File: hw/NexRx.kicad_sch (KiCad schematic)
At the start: 14 parts, among them J101 SMA, T101 INPUT

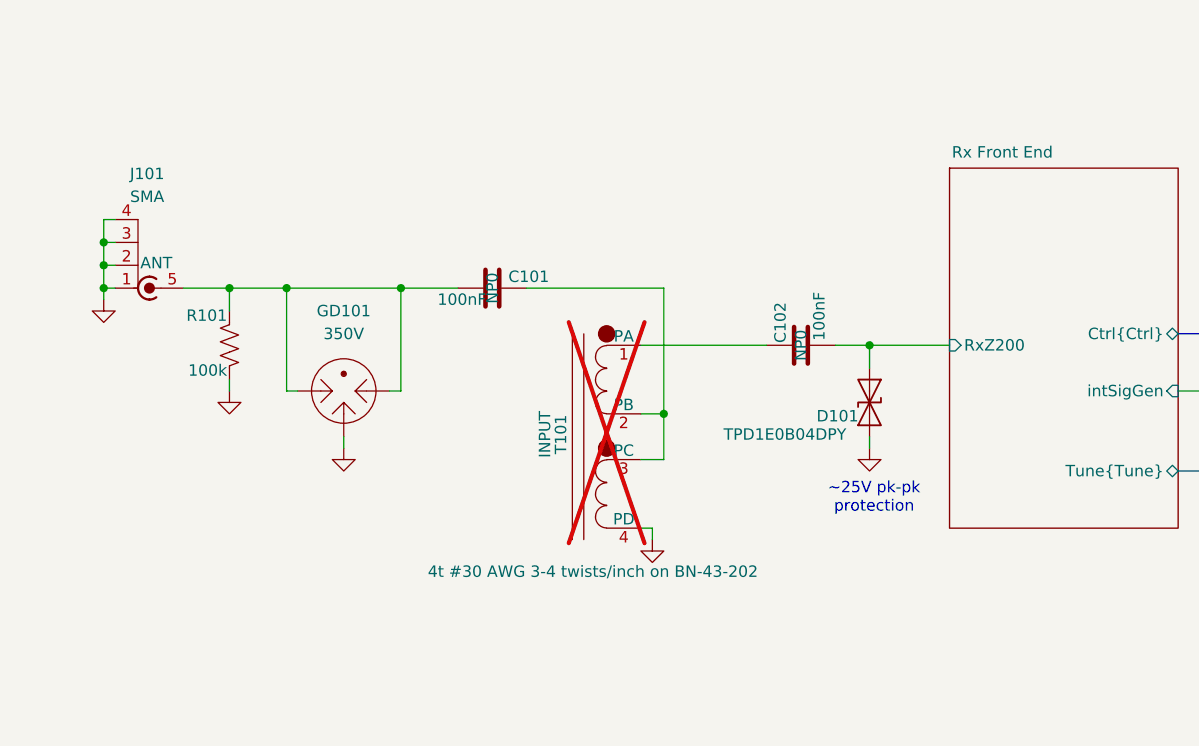
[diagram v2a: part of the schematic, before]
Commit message: Add filter-tester board project
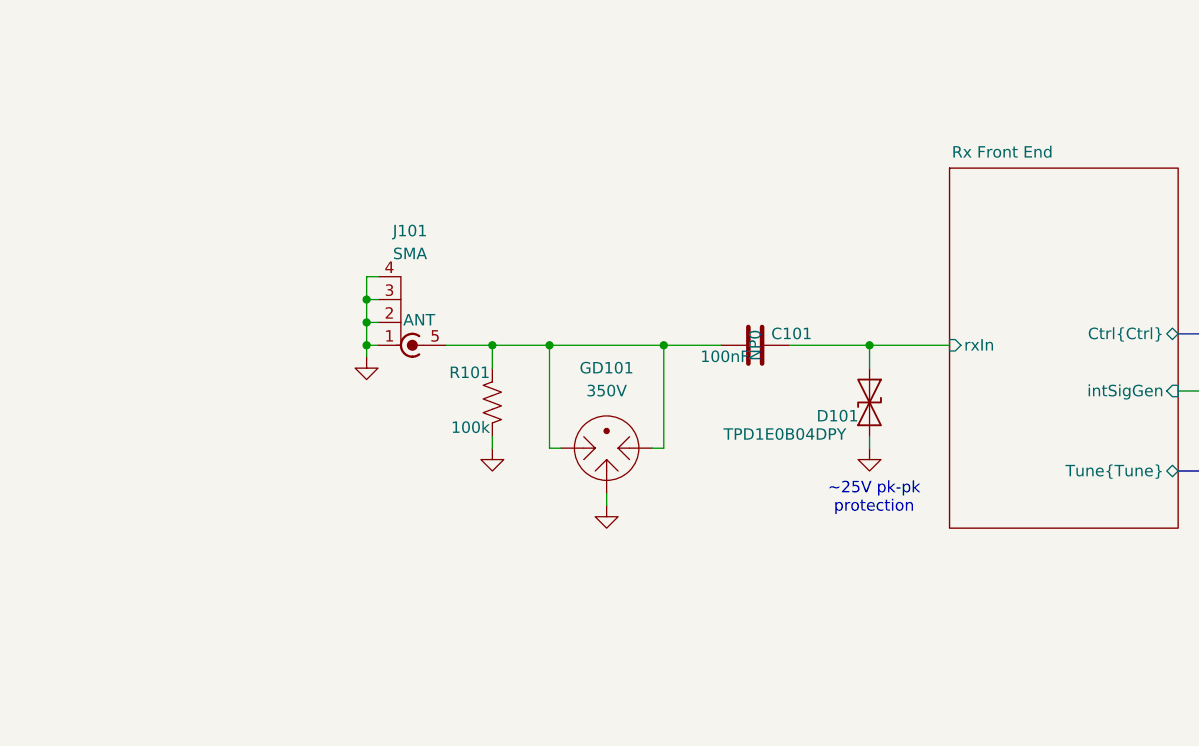
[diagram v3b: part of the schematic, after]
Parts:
- removed C102: 100nF, Capacitor_SMD:C_1206_3216Metric, symbol Device:C
- removed T101: INPUT, Library:Transformer-unun-BN-43-202, symbol Library:Ruthroff-2P
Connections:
- net Rx Front End/RxZ200 is gone; now on net Rx Front End/rxIn: D101.1 (A1)
- net Rx Front End/rxIn: now reaches C101.1
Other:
- sheet Rx Front End ports: added rxIn; removed RxZ200
- moved on the sheet: C101, GD101, J101, R101
